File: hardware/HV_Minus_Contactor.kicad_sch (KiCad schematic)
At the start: 15 parts

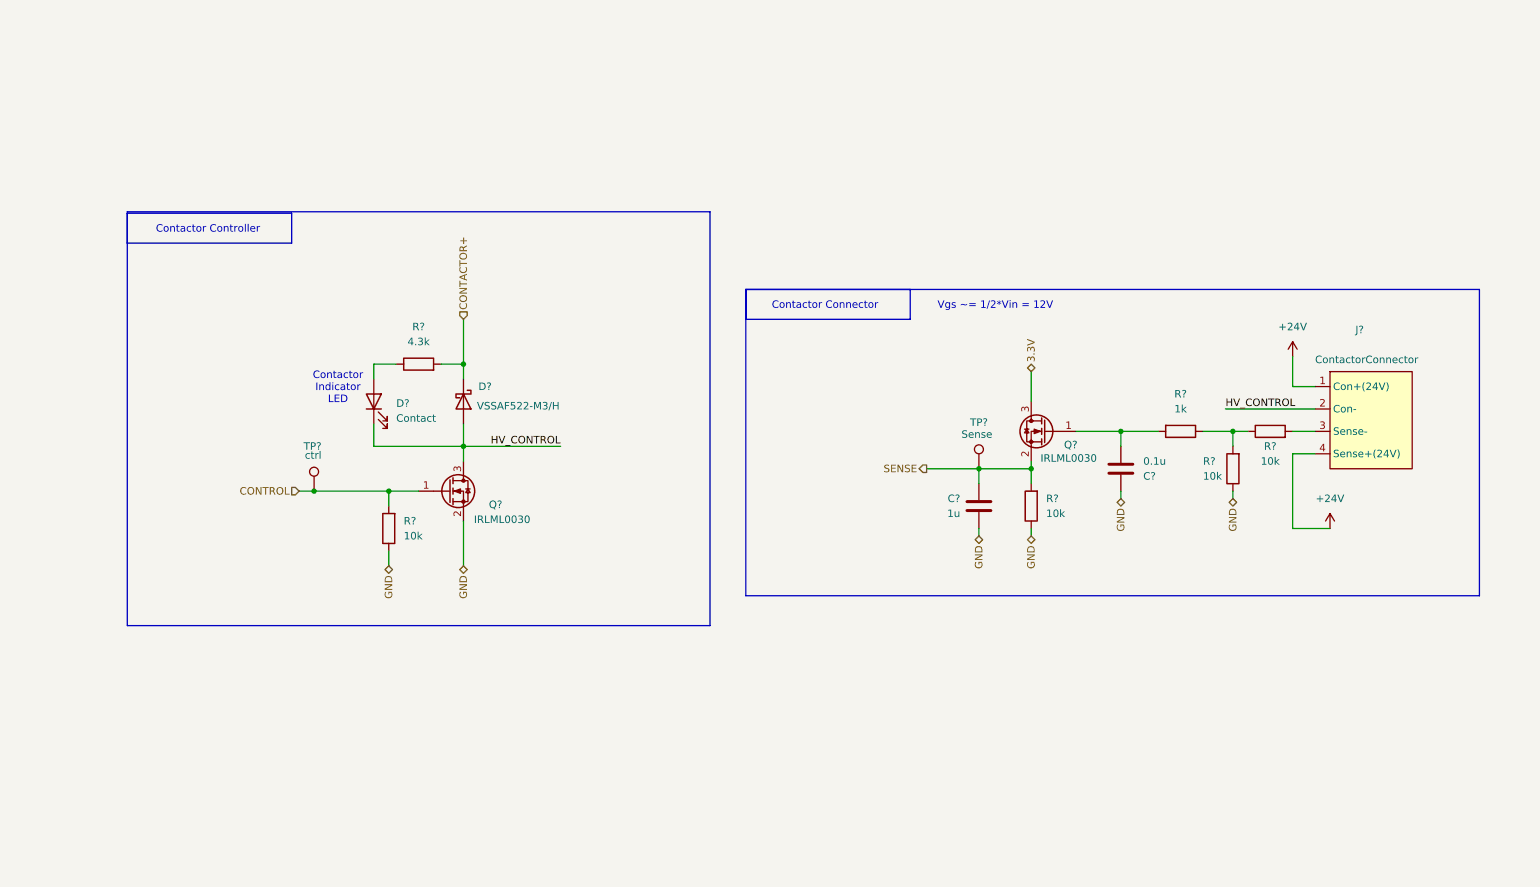
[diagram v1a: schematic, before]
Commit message: new contactor design block, started power mux
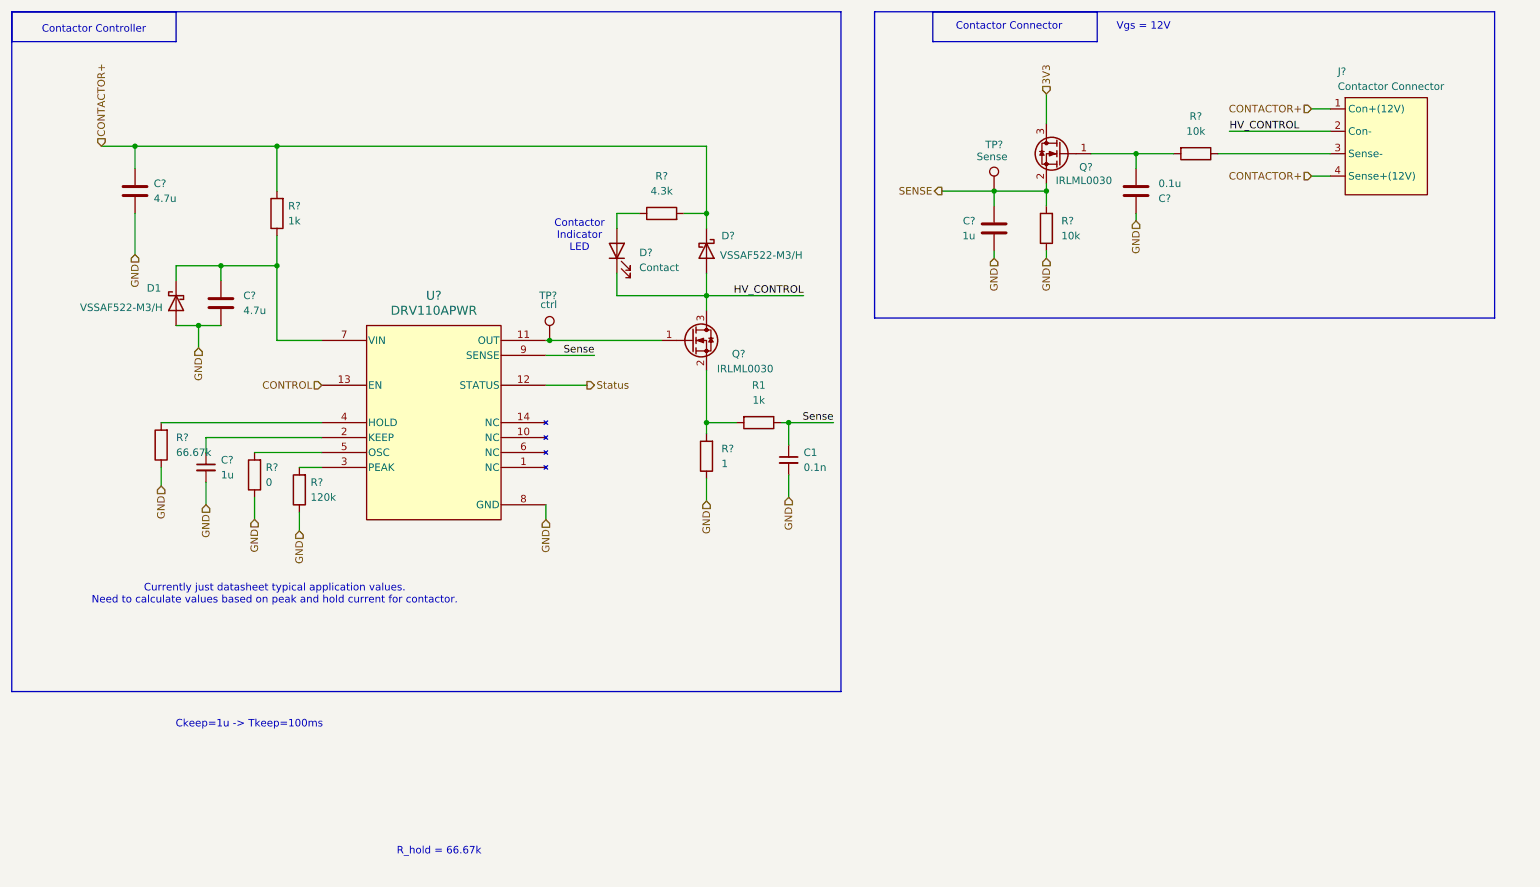
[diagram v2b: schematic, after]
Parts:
- removed C?: 0.1u, Capacitor_SMD:C_0603_1608Metric_Pad1.08x0.95mm_HandSolder, symbol Device:C
- removed D?: VSSAF522-M3/H, CustomKiCad-Library:SODFL5226X100N, symbol Diode:C3D25170H
- removed J?: ContactorConnector, UTSVT_Connectors:Molex_Nano-Fit_105309-xx04_1x04_P2.50mm_Vertical, symbol UTSVT_Connectors:ContactorConnector
- removed Q?: IRLML0030, Package_TO_SOT_SMD:SOT-23, symbol Transistor_FET:IRLML0030
- removed R? (x3): 10k, symbol Device:R
- removed R?: 4.3k, symbol Device:R
- removed TP?: ctrl, TestPoint:TestPoint_Pad_1.0x1.0mm, symbol Connector:TestPoint
- removed TP?: Sense, TestPoint:TestPoint_Pad_1.0x1.0mm, symbol Connector:TestPoint
- added C1: 0.1n, symbol Device:C_Small
- added C?: 0.1u, Capacitor_SMD:C_0603_1608Metric_Pad1.08x0.95mm_HandSolder, symbol Device:C
- added C? (x2): 4.7u, symbol Device:C
- added C?: 1u, symbol Device:C_Small
- added D1, D?: VSSAF522-M3/H, LHRS_Passives:SODFL5226X100N, symbol Diode:C3D25170H
- added J?: Contactor Connector, LHRS_Connectors:Molex_Nano-Fit_105309-xx04_1x04_P2.50mm_Vertical, symbol lhrs_connectors:ContactorConnector
- added Q?: IRLML0030, Package_TO_SOT_SMD:SOT-23, symbol Transistor_FET:IRLML0030
- added R1, R?: 1k, Resistor_SMD:R_0603_1608Metric_Pad0.98x0.95mm_HandSolder, symbol Device:R
- added R?: 120k, Resistor_SMD:R_0603_1608Metric_Pad0.98x0.95mm_HandSolder, symbol Device:R
- added R?: 0, Resistor_SMD:R_0603_1608Metric_Pad0.98x0.95mm_HandSolder, symbol Device:R
- added R?: 66.67k, Resistor_SMD:R_0603_1608Metric_Pad0.98x0.95mm_HandSolder, symbol Device:R
- added R?: 1, Resistor_SMD:R_0603_1608Metric_Pad0.98x0.95mm_HandSolder, symbol Device:R
- added R?: 4.3k, Resistor_SMD:R_0603_1608Metric_Pad0.98x0.95mm_HandSolder, symbol Device:R
- added TP?: Sense, TestPoint:TestPoint_THTPad_D3.0mm_Drill1.5mm, symbol Connector:TestPoint
- added TP?: ctrl, TestPoint:TestPoint_THTPad_D3.0mm_Drill1.5mm, symbol Connector:TestPoint
- added U?: DRV110APWR, PW14_TEX, symbol lhrs_ics:DRV110APWR
- R?: footprint (none) -> Resistor_SMD:R_0603_1608Metric_Pad0.98x0.95mm_HandSolder
- R?: value 1k -> 10k; footprint (none) -> Resistor_SMD:R_0603_1608Metric_Pad0.98x0.95mm_HandSolder
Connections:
- net CONTACTOR+: now also C?.1, D?.1 (K), J?.1 (Con+(12V)), J?.4 (Sense+(12V)), R?.2, R?.2
- net CONTROL: now also U?.13 (EN)
- net GND: now also C1.2, C?.1, C?.2, C?.2, C?.2, D1.2 (A), R?.1, R?.1, R?.1, R?.1, U?.8 (GND)
- net HV_CONTROL: now also D?.2 (A), J?.2 (Con-), Q?.3 (D)
- net SENSE: now also TP?.1
- net at D?.2 (A): now also R?.1
- net at R?.1: now also J?.3 (Sense-)
- net at Q?.1 (G), R?.2: now also C?.2
- net 3.3V renamed 3V3
- new net: R?.2, U?.3 (PEAK)
- new net: R?.2, U?.5 (OSC)
- new net: C?.1, D1.1 (K), R?.1, U?.7 (VIN)
- new net: Q?.1 (G), TP?.1, U?.11 (OUT)
- new net: C?.1, U?.2 (KEEP)
- new net: R?.2, U?.4 (HOLD)
- new net: Q?.2 (S), R1.2, R?.2
- new net Sense: C1.1, R1.1, U?.9 (SENSE)
- new net Status: U?.12 (STATUS)
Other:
- note added: "Ckeep=1u -> Tkeep=100ms"
- note added: "Currently just datasheet typical application values. Need to calculate values based on peak and hold current for contactor."
- note added: "R_hold = 66.67k"
- note added: "Vgs = 12V"
- note removed: "Vgs ~= 1/2*Vin = 12V"
- moved on the sheet: C?, D?, Q?, R?

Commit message: finished schematic except for 12v buck boost
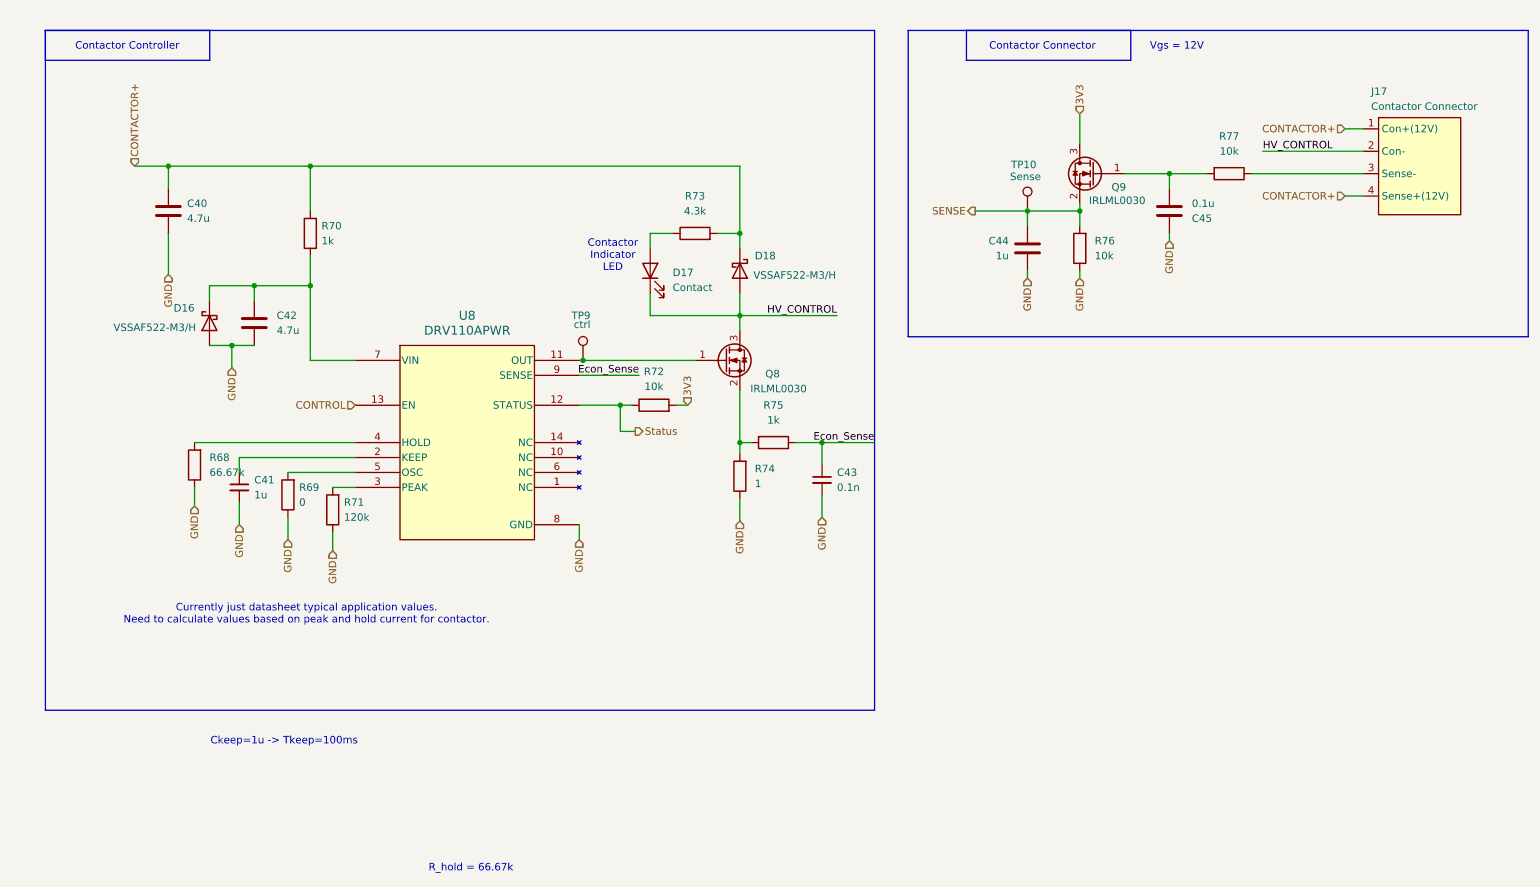
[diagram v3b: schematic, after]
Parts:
- removed C1: 0.1n, symbol Device:C_Small
- removed C?: 0.1u, Capacitor_SMD:C_0603_1608Metric_Pad1.08x0.95mm_HandSolder, symbol Device:C
- removed C? (x2): 4.7u, symbol Device:C
- removed C?: 1u, Capacitor_SMD:C_0603_1608Metric_Pad1.08x0.95mm_HandSolder, symbol Device:C
- removed C?: 1u, symbol Device:C_Small
- removed D1, D?: VSSAF522-M3/H, LHRS_Passives:SODFL5226X100N, symbol Diode:C3D25170H
- removed D?: Contact, LED_SMD:LED_0603_1608Metric, symbol Device:LED
- removed J?: Contactor Connector, LHRS_Connectors:Molex_Nano-Fit_105309-xx04_1x04_P2.50mm_Vertical, symbol lhrs_connectors:ContactorConnector
- removed Q? (x2): IRLML0030, Package_TO_SOT_SMD:SOT-23, symbol Transistor_FET:IRLML0030
- removed R1, R?: 1k, Resistor_SMD:R_0603_1608Metric_Pad0.98x0.95mm_HandSolder, symbol Device:R
- removed R?: 120k, Resistor_SMD:R_0603_1608Metric_Pad0.98x0.95mm_HandSolder, symbol Device:R
- removed R?: 0, Resistor_SMD:R_0603_1608Metric_Pad0.98x0.95mm_HandSolder, symbol Device:R
- removed R? (x2): 10k, Resistor_SMD:R_0603_1608Metric_Pad0.98x0.95mm_HandSolder, symbol Device:R
- removed R?: 66.67k, Resistor_SMD:R_0603_1608Metric_Pad0.98x0.95mm_HandSolder, symbol Device:R
- removed R?: 1, Resistor_SMD:R_0603_1608Metric_Pad0.98x0.95mm_HandSolder, symbol Device:R
- removed R?: 4.3k, Resistor_SMD:R_0603_1608Metric_Pad0.98x0.95mm_HandSolder, symbol Device:R
- removed TP?: Sense, TestPoint:TestPoint_THTPad_D3.0mm_Drill1.5mm, symbol Connector:TestPoint
- removed TP?: ctrl, TestPoint:TestPoint_THTPad_D3.0mm_Drill1.5mm, symbol Connector:TestPoint
- removed U?: DRV110APWR, PW14_TEX, symbol lhrs_ics:DRV110APWR
- added C40, C42: 4.7u, Capacitor_SMD:C_0805_2012Metric_Pad1.18x1.45mm_HandSolder, symbol Device:C
- added C41: 1u, Capacitor_SMD:C_0603_1608Metric_Pad1.08x0.95mm_HandSolder, symbol Device:C_Small
- added C43: 0.1n, Capacitor_SMD:C_0603_1608Metric_Pad1.08x0.95mm_HandSolder, symbol Device:C_Small
- added C44: 1u, Capacitor_SMD:C_0603_1608Metric_Pad1.08x0.95mm_HandSolder, symbol Device:C
- added C45: 0.1u, Capacitor_SMD:C_0603_1608Metric_Pad1.08x0.95mm_HandSolder, symbol Device:C
- added D16, D18: VSSAF522-M3/H, LHRS_Passives:SODFL5226X100N, symbol Diode:C3D25170H
- added D17: Contact, LED_SMD:LED_0603_1608Metric_Pad1.05x0.95mm_HandSolder, symbol Device:LED
- added J17: Contactor Connector, LHRS_Connectors:Molex_Nano-Fit_105309-xx04_1x04_P2.50mm_Vertical, symbol lhrs_connectors:ContactorConnector
- added Q8, Q9: IRLML0030, Package_TO_SOT_SMD:SOT-23, symbol Transistor_FET:IRLML0030
- added R68: 66.67k, Resistor_SMD:R_0603_1608Metric_Pad0.98x0.95mm_HandSolder, symbol Device:R
- added R69: 0, Resistor_SMD:R_0603_1608Metric_Pad0.98x0.95mm_HandSolder, symbol Device:R
- added R70, R75: 1k, Resistor_SMD:R_0603_1608Metric_Pad0.98x0.95mm_HandSolder, symbol Device:R
- added R71: 120k, Resistor_SMD:R_0603_1608Metric_Pad0.98x0.95mm_HandSolder, symbol Device:R
- added R72, R76, R77: 10k, Resistor_SMD:R_0603_1608Metric_Pad0.98x0.95mm_HandSolder, symbol Device:R
- added R73: 4.3k, Resistor_SMD:R_0603_1608Metric_Pad0.98x0.95mm_HandSolder, symbol Device:R
- added R74: 1, Resistor_SMD:R_0603_1608Metric_Pad0.98x0.95mm_HandSolder, symbol Device:R
- added TP10: Sense, TestPoint:TestPoint_THTPad_D3.0mm_Drill1.5mm, symbol Connector:TestPoint
- added TP9: ctrl, TestPoint:TestPoint_THTPad_D3.0mm_Drill1.5mm, symbol Connector:TestPoint
- added U8: DRV110APWR, LHRS_ICs:PW14_TEX, symbol lhrs_ics:DRV110APWR
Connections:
- net 3V3: now also Q9.3 (D), R72.2
- net CONTACTOR+: now also C40.1, D18.1 (K), J17.1 (Con+(12V)), J17.4 (Sense+(12V)), R70.2, R73.2
- net CONTROL: now also U8.13 (EN)
- net GND: now also C40.2, C41.2, C42.2, C43.2, C44.1, C45.1, D16.2 (A), R68.1, R69.1, R71.1, R74.1, R76.1, U8.8 (GND)
- net HV_CONTROL: now also D17.1 (K), D18.2 (A), J17.2 (Con-), Q8.3 (D)
- net SENSE: now also C44.2, Q9.2 (S), R76.2, TP10.1
- net Status: now also R72.1, U8.12 (STATUS)
- new net: C42.1, D16.1 (K), R70.1, U8.7 (VIN)
- new net: R71.2, U8.3 (PEAK)
- new net: Q8.1 (G), TP9.1, U8.11 (OUT)
- new net: C41.1, U8.2 (KEEP)
- new net: R68.2, U8.4 (HOLD)
- new net: R69.2, U8.5 (OSC)
- new net: C45.2, Q9.1 (G), R77.2
- new net: J17.3 (Sense-), R77.1
- new net: Q8.2 (S), R74.2, R75.2
- new net: D17.2 (A), R73.1
- new net Econ_Sense: C43.1, R75.1, U8.9 (SENSE)
